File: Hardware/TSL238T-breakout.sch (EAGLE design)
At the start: 4 parts, among them J1 CONN_42.54_NOSILK

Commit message: Labels, 3rd hole
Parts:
- added H3: (no value), bschulz:MOUNTING_HOLE2_NP
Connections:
- net N$1 renamed GND
- net N$2 renamed VDD
- net N$3 renamed OE
- net N$4 renamed OUT
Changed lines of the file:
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@@
 <?xml version="1.0" encoding="utf-8"?>
 <!DOCTYPE eagle SYSTEM "eagle.dtd">
-<eagle version="9.2.2">
+<eagle version="9.2.0">
 <drawing>
 <settings>
@@
 <part name="H2" library="bschulz" deviceset="MOUNTING_HOLE" device="2_NP"/>
 <part name="J1" library="bschulz" deviceset="CONN_4" device="2.54_NOSILK"/>
+<part name="H3" library="bschulz" deviceset="MOUNTING_HOLE" device="2_NP"/>
 </parts>
 <sheets>
@@
 </plain>
 <instances>
-<instance part="FRAME1" gate="G$1" x="0" y="0" smashed="yes"/>
-<instance part="FRAME1" gate="G$2" x="172.72" y="0" smashed="yes">
+<instance part="FRAME1" gate="G$1" x="0" y="0"/>
+<instance part="FRAME1" gate="G$2" x="172.72" y="0">
 <attribute name="LAST_DATE_TIME" x="185.42" y="1.27" size="2.54" layer="94"/>
 <attribute name="SHEET" x="259.08" y="1.27" size="2.54" layer="94"/>
 <attribute name="DRAWING_NAME" x="190.5" y="19.05" size="2.54" layer="94"/>
 </instance>
-<instance part="U$1" gate="G$1" x="152.4" y="114.3" smashed="yes">
+<instance part="U$1" gate="G$1" x="152.4" y="114.3">
 <attribute name="NAME" x="142.24" y="121.92" size="1.27" layer="95"/>
 </instance>
-<instance part="H1" gate="G$1" x="137.16" y="88.9" smashed="yes">
+<instance part="H1" gate="G$1" x="137.16" y="88.9">
 <attribute name="NAME" x="139.192" y="89.4842" size="1.778" layer="95"/>
 <attribute name="VALUE" x="139.192" y="86.4362" size="1.778" layer="96"/>
 </instance>
-<instance part="H2" gate="G$1" x="147.32" y="88.9" smashed="yes">
+<instance part="H2" gate="G$1" x="147.32" y="88.9">
 <attribute name="NAME" x="149.352" y="89.4842" size="1.778" layer="95"/>
 <attribute name="VALUE" x="149.352" y="86.4362" size="1.778" layer="96"/>
 </instance>
-<instance part="J1" gate="G$1" x="111.76" y="114.3" smashed="yes">
+<instance part="J1" gate="G$1" x="111.76" y="114.3">
 <attribute name="VALUE" x="96.52" y="106.934" size="1.778" layer="96" font="vector"/>
 <attribute name="NAME" x="106.68" y="122.428" size="1.778" layer="95" font="vector"/>
+</instance>
+<instance part="H3" gate="G$1" x="157.48" y="88.9">
+<attribute name="NAME" x="159.512" y="89.4842" size="1.778" layer="95"/>
+<attribute name="VALUE" x="159.512" y="86.4362" size="1.778" layer="96"/>
 </instance>
 </instances>
@@
 </busses>
 <nets>
-<net name="N$1" class="0">
+<net name="GND" class="0">
 <segment>
 <wire x1="137.16" y1="111.76" x2="127" y2="111.76" width="0.1524" layer="91"/>
@@
 <pinref part="U$1" gate="G$1" pin="GND"/>
 <pinref part="J1" gate="G$1" pin="2"/>
-</segment>
-</net>
-<net name="N$2" class="0">
+<label x="119.38" y="114.3" size="1.778" layer="95"/>
+</segment>
+</net>
+<net name="VDD" class="0">
 <segment>
 <wire x1="167.64" y1="111.76" x2="172.72" y2="111.76" width="0.1524" layer="91"/>
@@
 <pinref part="U$1" gate="G$1" pin="VDD"/>
 <pinref part="J1" gate="G$1" pin="1"/>
-</segment>
-</net>
-<net name="N$3" class="0">
+<label x="124.46" y="104.14" size="1.778" layer="95"/>
+</segment>
+</net>
+<net name="OE" class="0">
 <segment>
 <wire x1="137.16" y1="116.84" x2="116.84" y2="116.84" width="0.1524" layer="91"/>
 <pinref part="U$1" gate="G$1" pin="OE_INV"/>
 <pinref part="J1" gate="G$1" pin="3"/>
-</segment>
-</net>
-<net name="N$4" class="0">
+<label x="119.38" y="116.84" size="1.778" layer="95"/>
+</segment>
+</net>
+<net name="OUT" class="0">
 <segment>
 <wire x1="167.64" y1="116.84" x2="172.72" y2="116.84" width="0.1524" layer="91"/>
@@
 <pinref part="U$1" gate="G$1" pin="OUT"/>
 <pinref part="J1" gate="G$1" pin="4"/>
-</segment>
-</net>
+<label x="134.62" y="124.46" size="1.778" layer="95"/>
+</segment>
+</net>

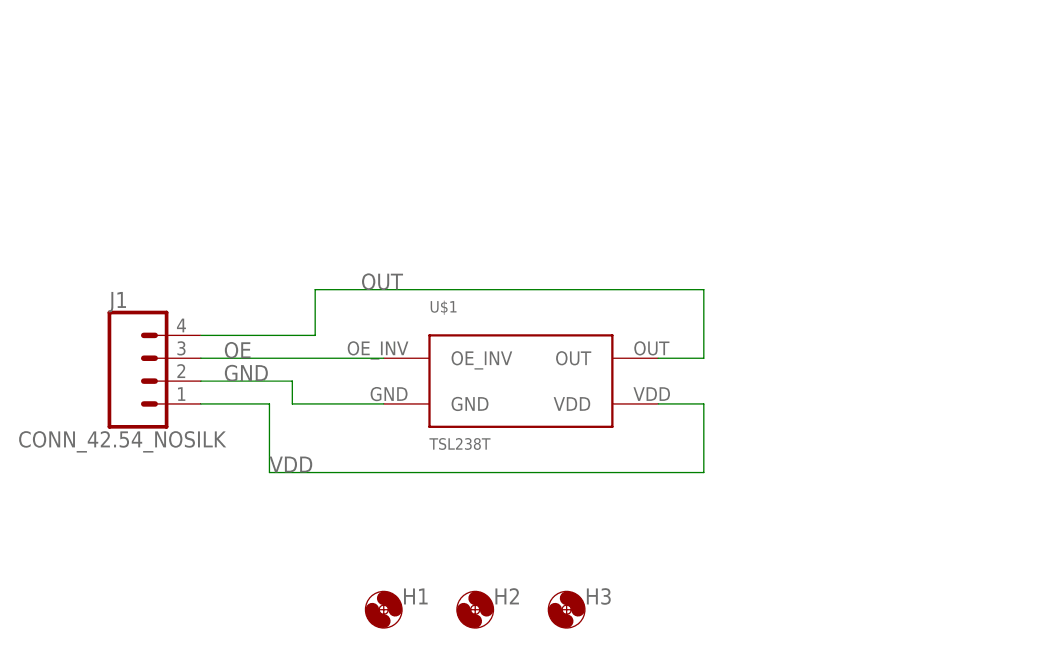
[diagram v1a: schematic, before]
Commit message: Updated breakouts and main board, schematic v0.1 updates
Updated schematic for main unit to v0.1, incorporating updates from testing of v0.0 unit
Minor updates to breakout boards, adding passives and updating components
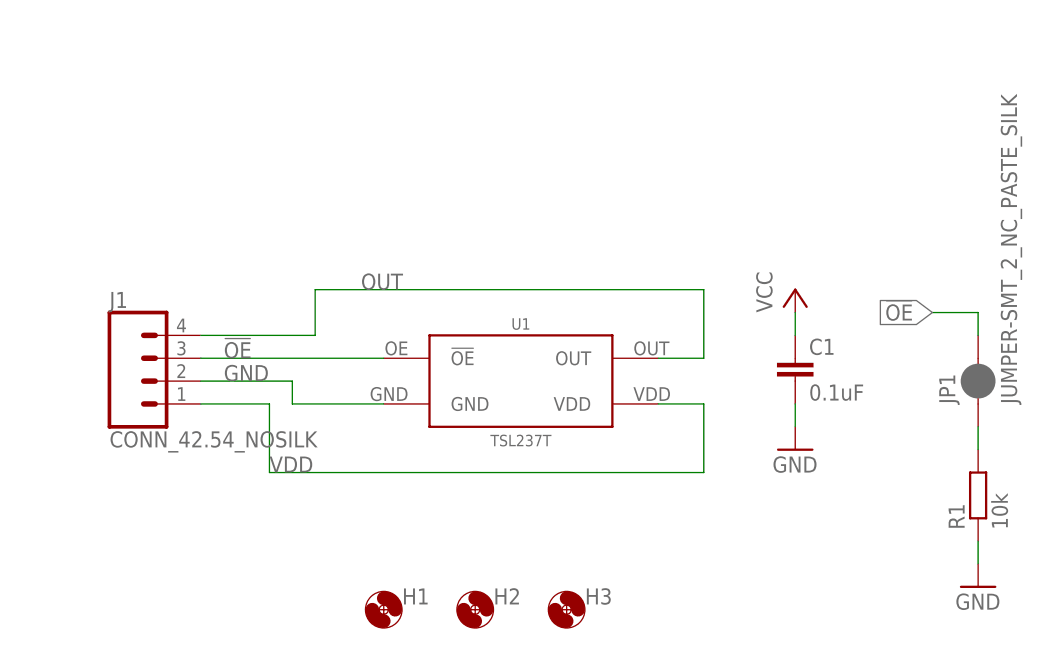
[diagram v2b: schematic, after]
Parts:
- removed U$1: TSL238T, bschulz:TSL238T
- added C1: 0.1uF, bschulz_passives:C-EU0.1UFC0402
- added JP1: JUMPER-SMT_2_NC_PASTE_SILK, SparkFun-Jumpers:JUMPER-SMT_2_NC_PASTE_SILK
- added R1: 10k, bschulz_passives:R-EU_10KR0402
- added U1: TSL237T, bschulz:TSL237T
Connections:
- removed net OE: J1.3, U$1.OE_INV
- new net !OE: J1.3, JP1.2, U1.!OE
- new net N$2: JP1.1, R1.2
- net GND: now also C1.2, R1.1, U1.GND; no longer U$1.GND
- net OUT: now also U1.OUT; no longer U$1.OUT
- net VDD: now also C1.1, U1.VDD; no longer U$1.VDD
